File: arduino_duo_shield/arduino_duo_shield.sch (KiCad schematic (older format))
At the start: 15 parts, among them J2 EStop, J3 Motor_Control, J4 Limit_Switches, J5 inverter_freq, J6 inverter_cmd, J8 inverter_power, J9 Motor_Control_Mirror, P10 Digital, P11 PWM, P12 PWM, P13 Communication, P7 Power, P8 Analog, P9 Analog, SW1 SW_Push

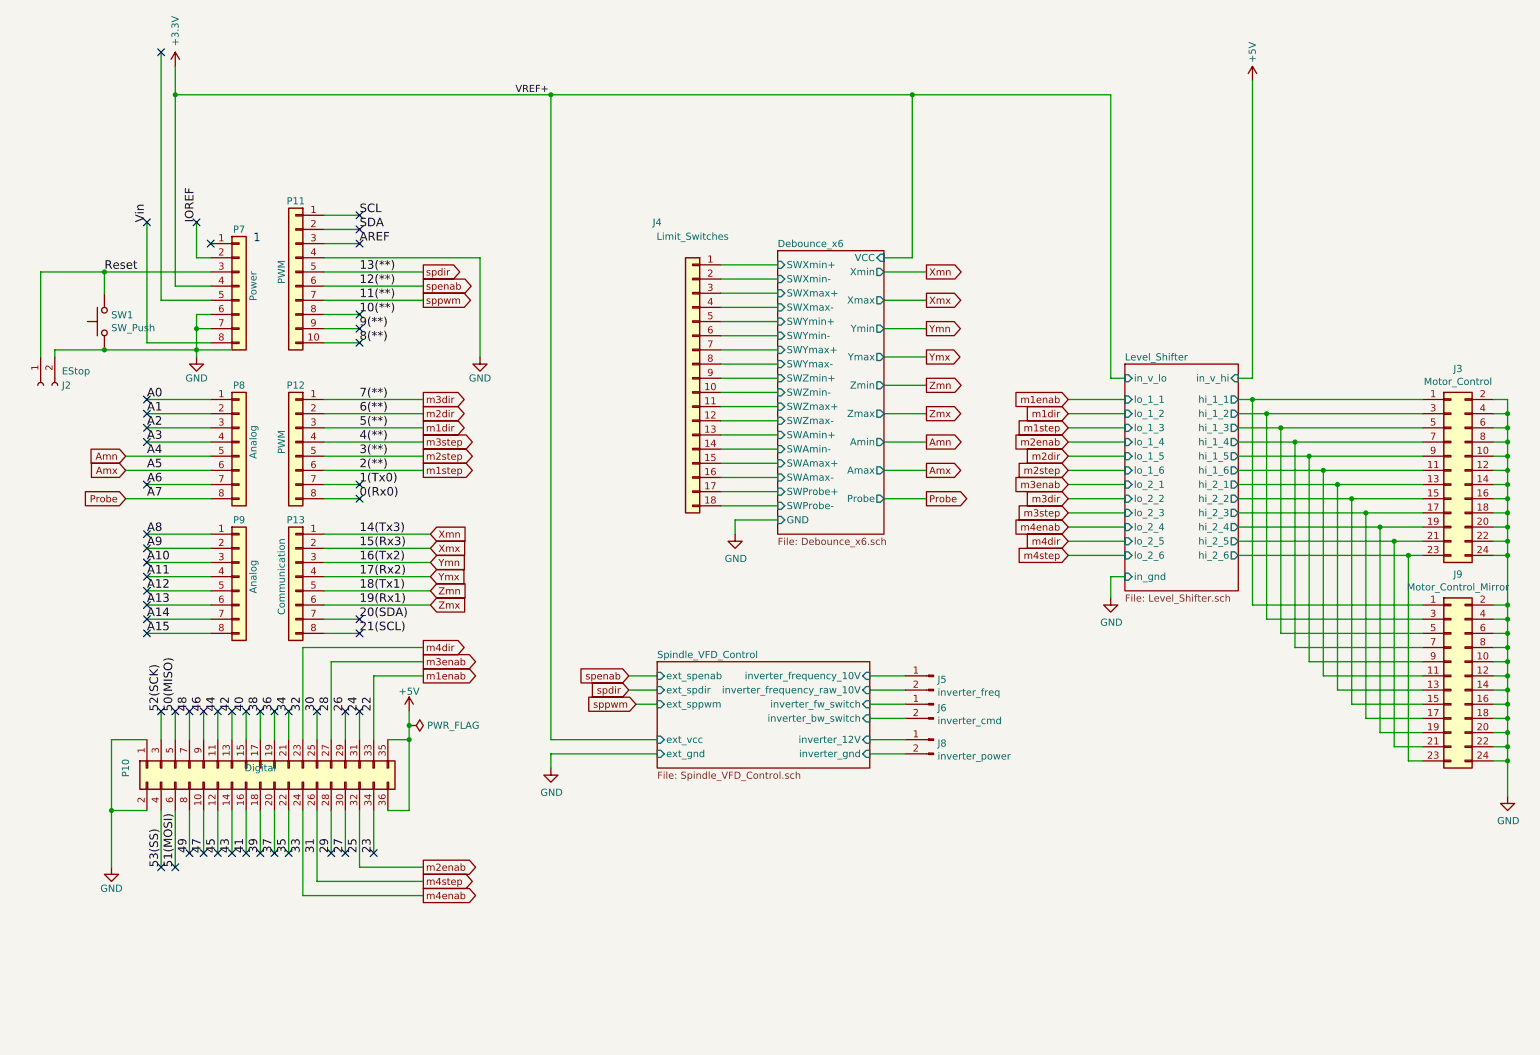
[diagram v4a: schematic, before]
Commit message: Add support for spindle estop
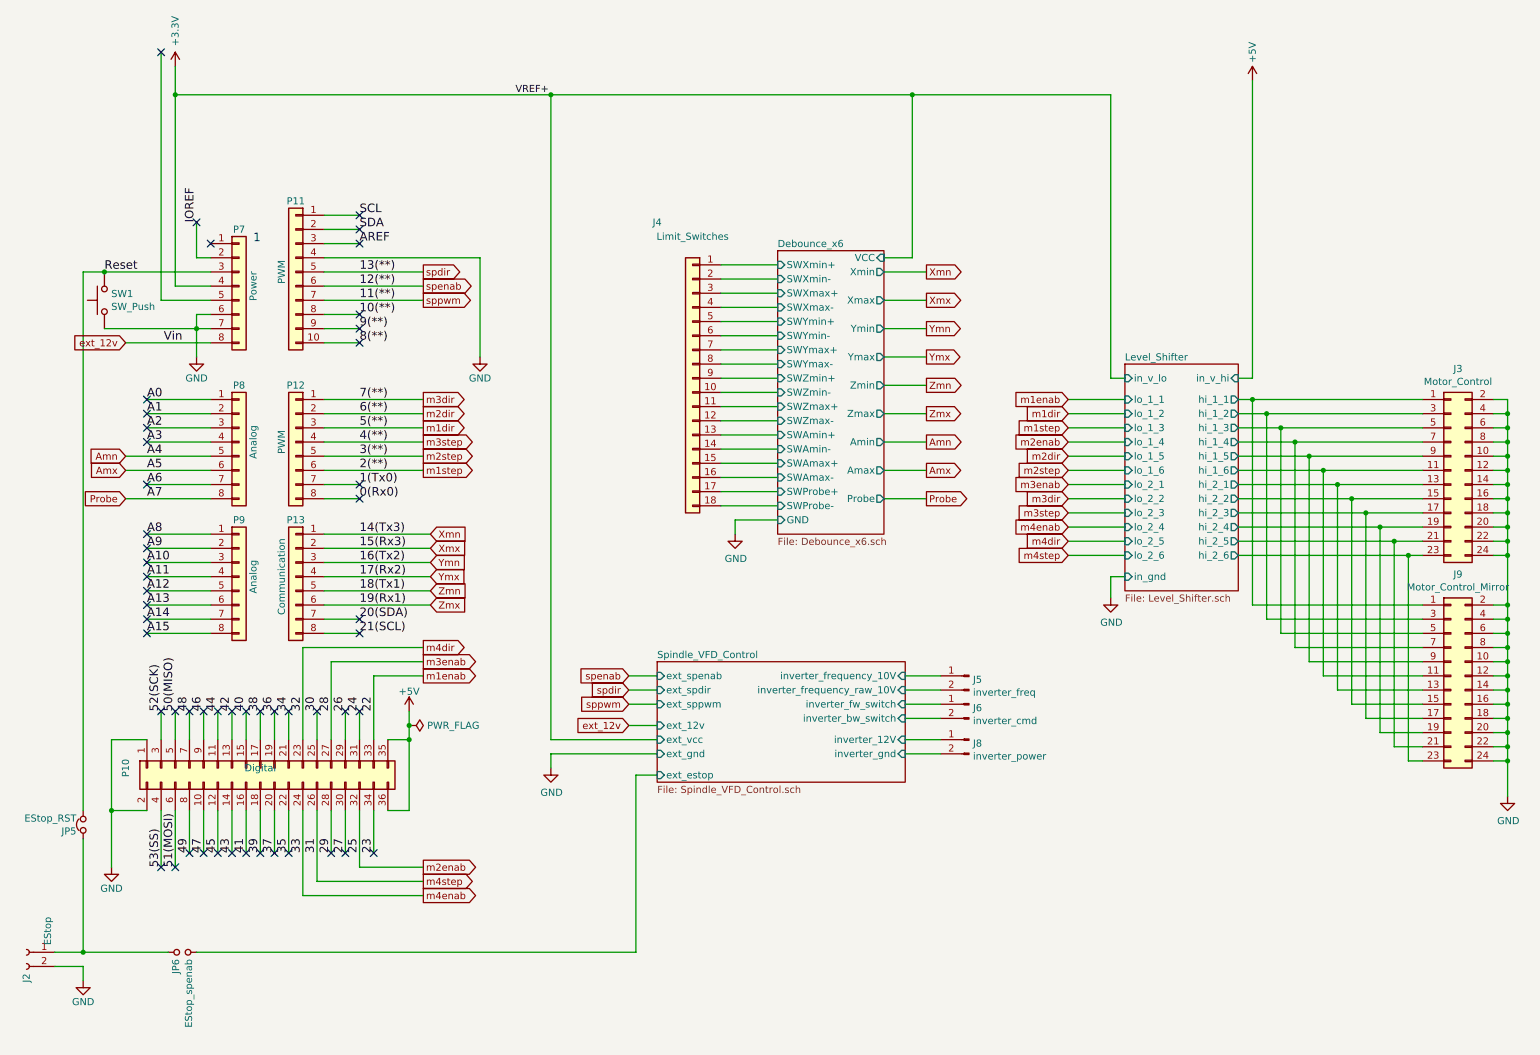
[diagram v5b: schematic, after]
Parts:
- added JP5: EStop_RST, Connector_PinHeader_2.54mm:PinHeader_1x02_P2.54mm_Vertical, symbol Device:Jumper_NC_Small
- added JP6: EStop_spenab, Connector_PinHeader_2.54mm:PinHeader_1x02_P2.54mm_Vertical, symbol Device:Jumper_NO_Small
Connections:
- net Reset: now also JP5.2; no longer J2.1 (Pin_1)
- net Vin renamed ext_12v
- new net: J2.1 (Pin_1), JP5.1, JP6.1
- new net Spindle_VFD_Control/ext_estop: JP6.2
- no-connect marks 53 -> 52
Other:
- moved on the sheet: J2, J5, J6, J8, SW1
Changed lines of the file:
@@
 Text Label 1850 2150 1    60   ~ 0
 IOREF
-Text Label 1500 2150 1    60   ~ 0
+Text Label 1750 3000 2    60   ~ 0
 Vin
 Text Label 1500 3400 0    60   ~ 0
@@
 	1600 2700 1950 2700
 Wire Wire Line
-	1950 3000 1500 3000
-Wire Wire Line
-	1500 3000 1500 2150
+	1950 3000 1350 3000
 Wire Wire Line
 	1950 2800 1850 2800
 Wire Wire Line
 	1850 2800 1850 2900
-Wire Wire Line
-	1850 2900 1850 3050
 Wire Wire Line
 	1950 2900 1850 2900
@@
 NoConn ~ 3000 2300
 NoConn ~ 2900 6600
-NoConn ~ 1500 2150
 NoConn ~ 1850 2150
 Wire Wire Line
@@
 Text GLabel 4900 5450 0    50   Input ~ 0
 spdir
-Text GLabel 4950 5550 0    50   Input ~ 0
+Text GLabel 4900 5550 0    50   Input ~ 0
 sppwm
 $Comp
@@
 	4350 5900 4350 6000
 Wire Wire Line
-	5100 5550 4950 5550
+	5100 5550 4900 5550
 Wire Wire Line
 	1500 5800 1250 5800
@@
 Wire Wire Line
 	3350 5600 3350 5700
-Connection ~ 1850 3050
-Wire Wire Line
-	1850 3050 1850 3100
-Wire Wire Line
-	1200 2500 1200 2650
 $Comp
 L Switch:SW_Push SW1
 U 1 1 5DB555D9
-P 1200 2850
-F 0 "SW1" V 1246 2802 50  0000 R CNN
-F 1 "SW_Push" V 1155 2802 50  0000 R CNN
-F 2 "Button_Switch_THT:SW_PUSH_6mm" H 1200 3050 50  0001 C CNN
-F 3 "~" H 1200 3050 50  0001 C CNN
-	1    1200 2850
+P 1200 2700
+F 0 "SW1" V 1246 2652 50  0000 R CNN
+F 1 "SW_Push" V 1155 2652 50  0000 R CNN
+F 2 "Button_Switch_THT:SW_PUSH_6mm" H 1200 2900 50  0001 C CNN
+F 3 "~" H 1200 2900 50  0001 C CNN
+	1    1200 2700
 	0    -1   -1   0
 $EndComp
 Wire Wire Line
-	1200 3050 1850 3050
+	1200 2900 1850 2900
 $Comp
 L power:PWR_FLAG #FLG0104
@@
 	1600 950  1600 2700
 NoConn ~ 1600 950
-$Sheet
-S 5100 5250 1500 750
-U 5DD17641
-F0 "Spindle_VFD_Control" 50
-F1 "Spindle_VFD_Control.sch" 50
-F2 "inverter_12V" I R 6600 5800 50
-F3 "inverter_frequency_10V" I R 6600 5350 50
-F4 "ext_sppwm" I L 5100 5550 50
-F5 "ext_gnd" I L 5100 5900 50
-F6 "ext_spdir" I L 5100 5450 50
-F7 "ext_vcc" I L 5100 5800 50
-F8 "ext_spenab" I L 5100 5350 50
-F9 "inverter_fw_switch" I R 6600 5550 50
-F10 "inverter_bw_switch" I R 6600 5650 50
-F11 "inverter_gnd" I R 6600 5900 50
-F12 "inverter_frequency_raw_10V" I R 6600 5450 50
-$EndSheet
 Text GLabel 3450 2500 2    50   Output ~ 0
 spdir
 Wire Wire Line
 	2750 2500 3450 2500
-Text GLabel 4900 5350 0    50   Input ~ 0
-spenab
 Wire Wire Line
 	5100 5450 4900 5450
@@
 Wire Wire Line
 	11100 5950 11100 6200
-Wire Wire Line
-	1850 3050 2100 3050
 $Comp
 L Connector:Conn_01x02_Female J2
 U 1 1 5E163504
-P 750 3300
-F 0 "J2" V 750 3150 50  0000 R CNN
-F 1 "EStop" V 650 3150 50  0000 R CNN
-F 2 "TerminalBlock:TerminalBlock_bornier-2_P5.08mm" H 750 3300 50  0001 C CNN
-F 3 "~" H 750 3300 50  0001 C CNN
-	1    750  3300
-	0    -1   1    0
-$EndComp
-Wire Wire Line
-	850  3100 850  3050
-Wire Wire Line
-	850  3050 1200 3050
-Connection ~ 1200 3050
-Wire Wire Line
-	750  3100 750  2500
-Wire Wire Line
-	750  2500 1200 2500
-Connection ~ 1200 2500
+P 650 7300
+F 0 "J2" V 650 7150 50  0000 R CNN
+F 1 "EStop" V 500 7550 50  0000 R CNN
+F 2 "TerminalBlock:TerminalBlock_bornier-2_P5.08mm" H 650 7300 50  0001 C CNN
+F 3 "~" H 650 7300 50  0001 C CNN
+	1    650  7300
+	-1   0    0    -1
+$EndComp
 Wire Wire Line
 	9300 3400 9300 4850
@@
 L Connector:Conn_01x02_Male J?
 U 1 1 5E2A7440
-P 7050 5800
+P 7300 5800
 AR Path="/5D7DFDC0/5E2A7440" Ref="J?"  Part="1"
 AR Path="/5E2A7440" Ref="J8"  Part="1"
-F 0 "J8" H 7022 5774 50  0000 R CNN
-F 1 "inverter_power" H 7022 5683 50  0000 R CNN
-F 2 "TerminalBlock:TerminalBlock_bornier-2_P5.08mm" H 7050 5800 50  0001 C CNN
-F 3 "~" H 7050 5800 50  0001 C CNN
-	1    7050 5800
+F 0 "J8" H 7272 5774 50  0000 R CNN
+F 1 "inverter_power" H 7272 5683 50  0000 R CNN
+F 2 "TerminalBlock:TerminalBlock_bornier-2_P5.08mm" H 7300 5800 50  0001 C CNN
+F 3 "~" H 7300 5800 50  0001 C CNN
+	1    7300 5800
 	-1   0    0    -1
 $EndComp
 Wire Wire Line
-	6600 5550 6850 5550
-Wire Wire Line
-	6600 5650 6850 5650
+	6850 5550 7100 5550
+Wire Wire Line
+	6850 5650 7100 5650
 $Comp
 L Connector:Conn_01x02_Male J?
 U 1 1 5E2CBC81
-P 7050 5350
+P 7300 5350
 AR Path="/5D7DFDC0/5E2CBC81" Ref="J?"  Part="1"
 AR Path="/5E2CBC81" Ref="J5"  Part="1"
-F 0 "J5" H 7022 5324 50  0000 R CNN
-F 1 "inverter_freq" H 7022 5233 50  0000 R CNN
-F 2 "TerminalBlock:TerminalBlock_bornier-2_P5.08mm" H 7050 5350 50  0001 C CNN
-F 3 "~" H 7050 5350 50  0001 C CNN
-	1    7050 5350
+F 0 "J5" H 7272 5324 50  0000 R CNN
+F 1 "inverter_freq" H 7272 5233 50  0000 R CNN
+F 2 "TerminalBlock:TerminalBlock_bornier-2_P5.08mm" H 7300 5350 50  0001 C CNN
+F 3 "~" H 7300 5350 50  0001 C CNN
+	1    7300 5350
 	-1   0    0    -1
 $EndComp
@@
 L Connector:Conn_01x02_Male J?
 U 1 1 5E2B9818
-P 7050 5550
+P 7300 5550
 AR Path="/5D7DFDC0/5E2B9818" Ref="J?"  Part="1"
 AR Path="/5E2B9818" Ref="J6"  Part="1"
-F 0 "J6" H 7022 5524 50  0000 R CNN
-F 1 "inverter_cmd" H 7022 5433 50  0000 R CNN
-F 2 "TerminalBlock:TerminalBlock_bornier-2_P5.08mm" H 7050 5550 50  0001 C CNN
-F 3 "~" H 7050 5550 50  0001 C CNN
-	1    7050 5550
+F 0 "J6" H 7272 5524 50  0000 R CNN
+F 1 "inverter_cmd" H 7272 5433 50  0000 R CNN
+F 2 "TerminalBlock:TerminalBlock_bornier-2_P5.08mm" H 7300 5550 50  0001 C CNN
+F 3 "~" H 7300 5550 50  0001 C CNN
+	1    7300 5550
 	-1   0    0    -1
 $EndComp
@@
 	1200 2500 1950 2500
 Wire Wire Line
-	6850 5350 6600 5350
-Wire Wire Line
-	6600 5900 6850 5900
-Wire Wire Line
-	6600 5800 6850 5800
-Wire Wire Line
-	6600 5450 6850 5450
+	7100 5350 6850 5350
+Wire Wire Line
+	6850 5900 7100 5900
+Wire Wire Line
+	6850 5800 7100 5800
+Wire Wire Line
+	6850 5450 7100 5450
+Text GLabel 1350 3000 0    50   Input ~ 0
+ext_12v
+Text GLabel 4900 5700 0    50   Input ~ 0
+ext_12v
+Wire Wire Line
+	4900 5700 5100 5700
+Wire Wire Line
+	1850 2900 1850 3100
+$Sheet
+S 5100 5250 1750 850
+U 5DD17641
+F0 "Spindle_VFD_Control" 50
+F1 "Spindle_VFD_Control.sch" 50
+F2 "inverter_12V" I R 6850 5800 50
+F3 "inverter_frequency_10V" I R 6850 5350 50
+F4 "ext_sppwm" I L 5100 5550 50
+F5 "ext_gnd" I L 5100 5900 50
+F6 "ext_spdir" I L 5100 5450 50
+F7 "ext_vcc" I L 5100 5800 50
+F8 "ext_spenab" I L 5100 5350 50
+F9 "inverter_fw_switch" I R 6850 5550 50
+F10 "inverter_bw_switch" I R 6850 5650 50
+F11 "inverter_gnd" I R 6850 5900 50
+F12 "inverter_frequency_raw_10V" I R 6850 5450 50
+F13 "ext_12v" I L 5100 5700 50
+F14 "ext_estop" I L 5100 6050 50
+$EndSheet
+$Comp
+L power:GND #PWR02
+U 1 1 5E3CDF54
+P 1050 7500
+F 0 "#PWR02" H 1050 7250 50  0001 C CNN
+F 1 "GND" H 1050 7350 50  0000 C CNN
+F 2 "" H 1050 7500 50  0000 C CNN
+F 3 "" H 1050 7500 50  0000 C CNN
+	1    1050 7500
+	1    0    0    -1
+$EndComp
+Wire Wire Line
+	850  7300 1050 7300
+Wire Wire Line
+	850  7400 1050 7400
+Wire Wire Line
+	1050 7400 1050 7500
+Wire Wire Line
+	1200 2500 1050 2500
+Wire Wire Line
+	1050 2500 1050 6300
+Connection ~ 1200 2500
+Wire Wire Line
+	5100 6050 4950 6050
+Wire Wire Line
+	4950 6050 4950 7300
+Text GLabel 4900 5350 0    50   Input ~ 0
+spenab
+$Comp
+L Device:Jumper_NO_Small JP?
+U 1 1 5E474B40
+P 1750 7300
+AR Path="/5DD17641/5E474B40" Ref="JP?"  Part="1"
+AR Path="/5E474B40" Ref="JP6"  Part="1"
+F 0 "JP6" V 1704 7348 50  0000 L CNN
+F 1 "EStop_spenab" V 1795 7348 50  0000 L CNN
+F 2 "Connector_PinHeader_2.54mm:PinHeader_1x02_P2.54mm_Vertical" H 1750 7300 50  0001 C CNN
+F 3 "~" H 1750 7300 50  0001 C CNN
+	1    1750 7300
+	1    0    0    1
+$EndComp
+Connection ~ 1050 7300
+Wire Wire Line
+	1050 7300 1650 7300
+Wire Wire Line
+	1850 7300 4950 7300
+$Comp
+L Device:Jumper_NC_Small JP?
+U 1 1 5E489F3C
+P 1050 6400
+AR Path="/5DD17641/5E489F3C" Ref="JP?"  Part="1"
+AR Path="/5E489F3C" Ref="JP5"  Part="1"
+F 0 "JP5" V 1004 6448 50  0000 L CNN
+F 1 "EStop_RST" V 1095 6448 50  0000 L CNN
+F 2 "Connector_PinHeader_2.54mm:PinHeader_1x02_P2.54mm_Vertical" H 1050 6400 50  0001 C CNN
+F 3 "~" H 1050 6400 50  0001 C CNN
+	1    1050 6400
+	0    -1   -1   0
+$EndComp
+Wire Wire Line
+	1050 6500 1050 7300
 $EndSCHEMATC

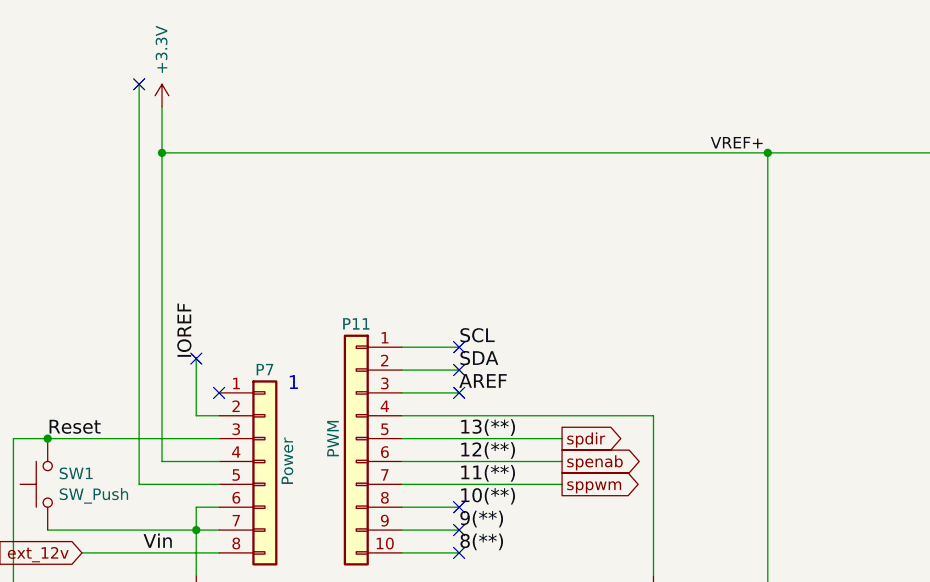
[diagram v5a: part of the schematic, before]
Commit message: Add support for 24LC16 EEPROM
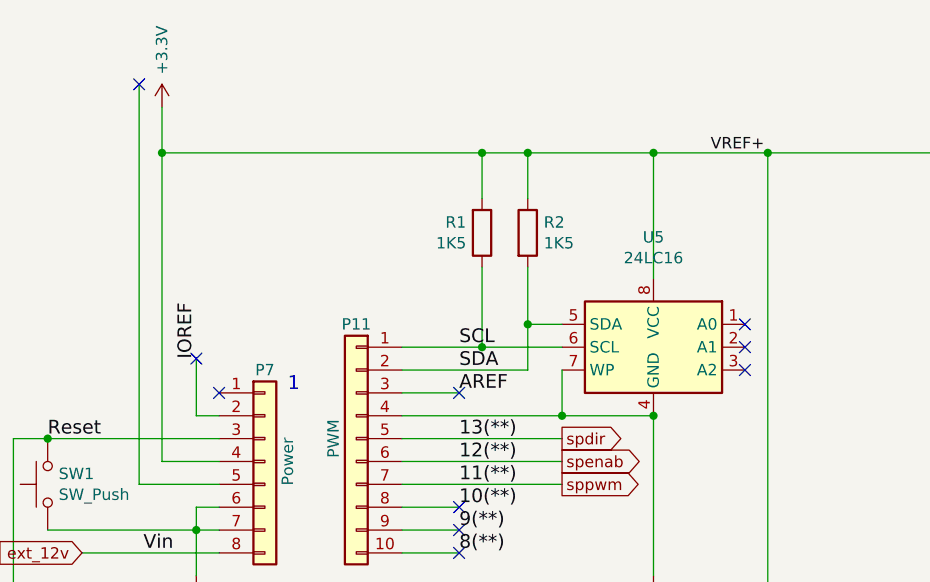
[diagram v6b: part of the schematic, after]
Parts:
- added R1, R2: 1K5, Resistor_THT:R_Axial_DIN0207_L6.3mm_D2.5mm_P7.62mm_Horizontal, symbol Device:R
- added U5: 24LC16, Package_DIP:DIP-8_W7.62mm_Socket, symbol Memory_EEPROM:24LC16
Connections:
- net +3V3: now also R1.2, R2.1, U5.8 (VCC)
- net GND: now also U5.4 (GND), U5.7 (WP)
- net SCL: now also R1.1, U5.6 (SCL)
- net SDA: now also R2.2, U5.5 (SDA)
- no-connect marks 52 -> 53
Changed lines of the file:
@@
 Connection ~ 1850 2900
 Wire Wire Line
-	2750 2100 3000 2100
-Wire Wire Line
-	3000 2200 2750 2200
-Wire Wire Line
 	2750 2300 3000 2300
 Wire Wire Line
@@
 	3850 3100 3850 2400
 Wire Wire Line
-	3850 2400 2750 2400
+	3850 2400 3450 2400
 Wire Wire Line
 	1950 3400 1500 3400
@@
 NoConn ~ 3000 3000
 NoConn ~ 3000 2800
-NoConn ~ 3000 2100
-NoConn ~ 3000 2200
+NoConn ~ 4250 2000
+NoConn ~ 4250 2100
 NoConn ~ 3000 2300
 NoConn ~ 2900 6600
@@
 	4350 5800 4350 1250
 Wire Wire Line
-	1700 1250 4350 1250
+	1700 1250 3100 1250
 $Sheet
 S 8400 3150 800  1600
@@
 Wire Wire Line
 	1050 6500 1050 7300
+$Comp
+L Memory_EEPROM:24LC16 U5
+U 1 1 5E39E512
+P 3850 2100
+F 0 "U5" H 3850 2581 50  0000 C CNN
+F 1 "24LC16" H 3850 2490 50  0000 C CNN
+F 2 "Package_DIP:DIP-8_W7.62mm_Socket" H 3850 2100 50  0001 C CNN
+F 3 "http://ww1.microchip.com/downloads/en/DeviceDoc/21703d.pdf" H 3850 2100 50  0001 C CNN
+	1    3850 2100
+	-1   0    0    -1
+$EndComp
+Connection ~ 3850 2400
+NoConn ~ 4250 2200
+Wire Wire Line
+	3850 1800 3850 1250
+Connection ~ 3850 1250
+Wire Wire Line
+	3850 1250 4350 1250
+Wire Wire Line
+	3300 2200 3300 2000
+Wire Wire Line
+	3300 2000 3450 2000
+Wire Wire Line
+	2750 2200 3300 2200
+Wire Wire Line
+	2750 2100 3100 2100
+Wire Wire Line
+	3450 2200 3450 2400
+Connection ~ 3450 2400
+Wire Wire Line
+	3450 2400 2750 2400
+$Comp
+L Device:R R2
+U 1 1 5E415F52
+P 3300 1600
+F 0 "R2" H 3370 1646 50  0000 L CNN
+F 1 "1K5" H 3370 1555 50  0000 L CNN
+F 2 "Resistor_THT:R_Axial_DIN0207_L6.3mm_D2.5mm_P7.62mm_Horizontal" V 3230 1600 50  0001 C CNN
+F 3 "~" H 3300 1600 50  0001 C CNN
+	1    3300 1600
+	1    0    0    -1
+$EndComp
+$Comp
+L Device:R R1
+U 1 1 5E416810
+P 3100 1600
+F 0 "R1" H 3031 1554 50  0000 R CNN
+F 1 "1K5" H 3031 1645 50  0000 R CNN
+F 2 "Resistor_THT:R_Axial_DIN0207_L6.3mm_D2.5mm_P7.62mm_Horizontal" V 3030 1600 50  0001 C CNN
+F 3 "~" H 3100 1600 50  0001 C CNN
+	1    3100 1600
+	1    0    0    1
+$EndComp
+Wire Wire Line
+	3300 1250 3300 1450
+Connection ~ 3300 1250
+Wire Wire Line
+	3300 1250 3850 1250
+Wire Wire Line
+	3100 1250 3100 1450
+Connection ~ 3100 1250
+Wire Wire Line
+	3100 1250 3300 1250
+Wire Wire Line
+	3300 1750 3300 2000
+Connection ~ 3300 2000
+Wire Wire Line
+	3100 1750 3100 2100
+Connection ~ 3100 2100
+Wire Wire Line
+	3100 2100 3450 2100
 $EndSCHEMATC
